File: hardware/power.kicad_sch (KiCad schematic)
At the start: 64 parts, among them IC1 LMR38020FDDAR, Q1 LMR51635XDDCR, Q2 LMR51635XDDCR, U3 LM1117-3.3

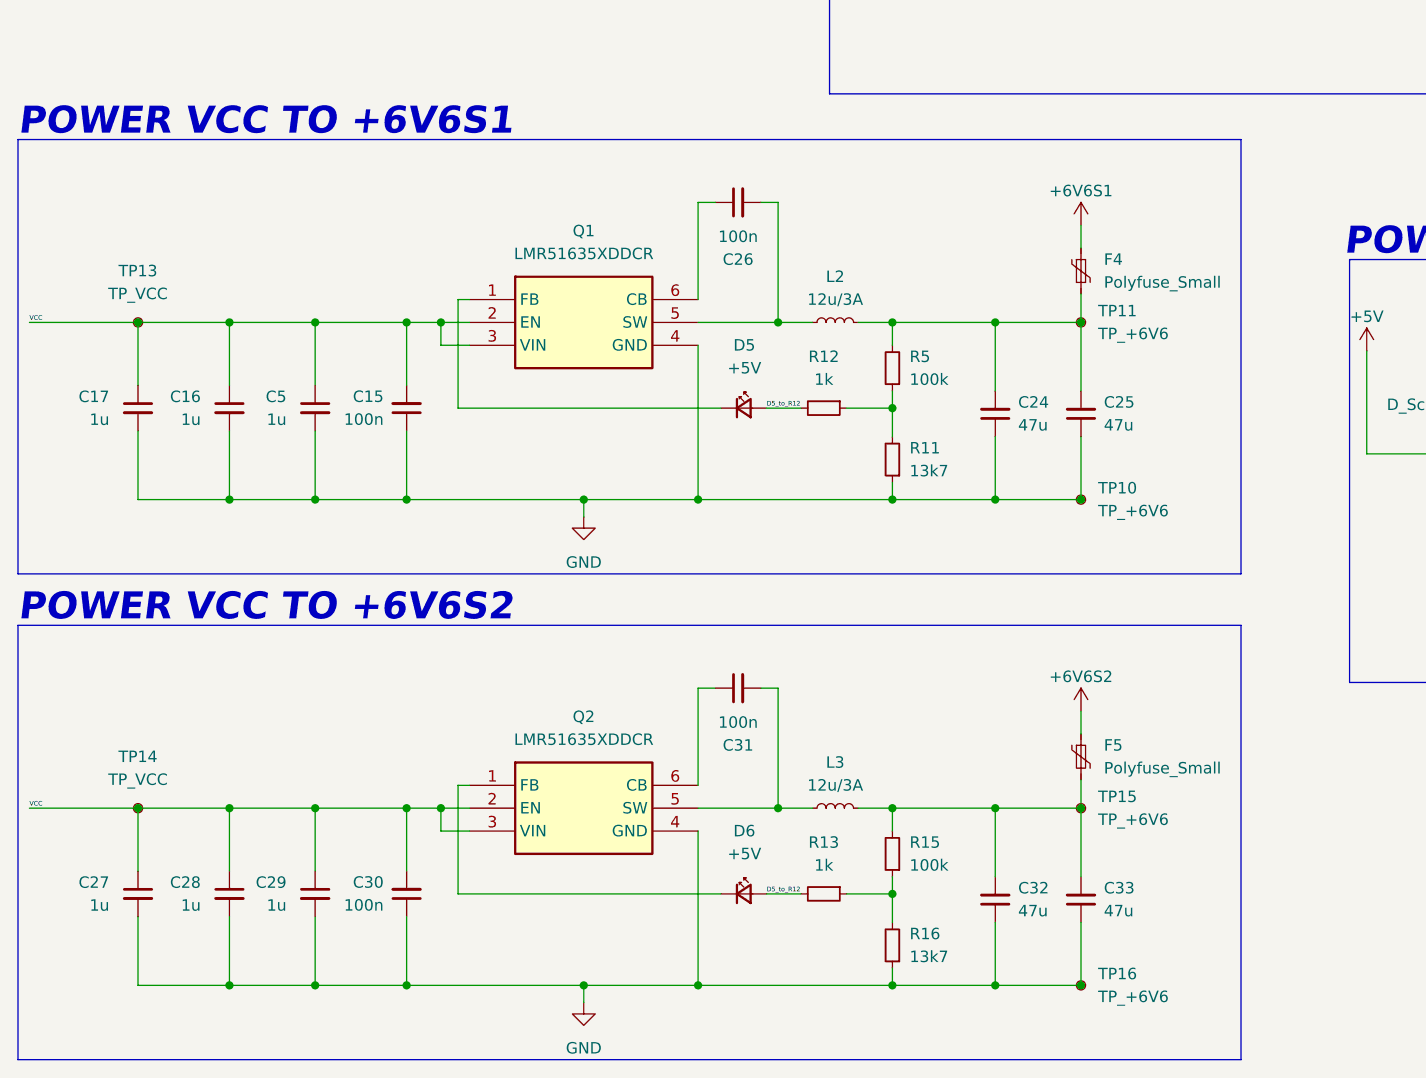
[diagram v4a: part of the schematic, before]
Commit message: power labels corrected
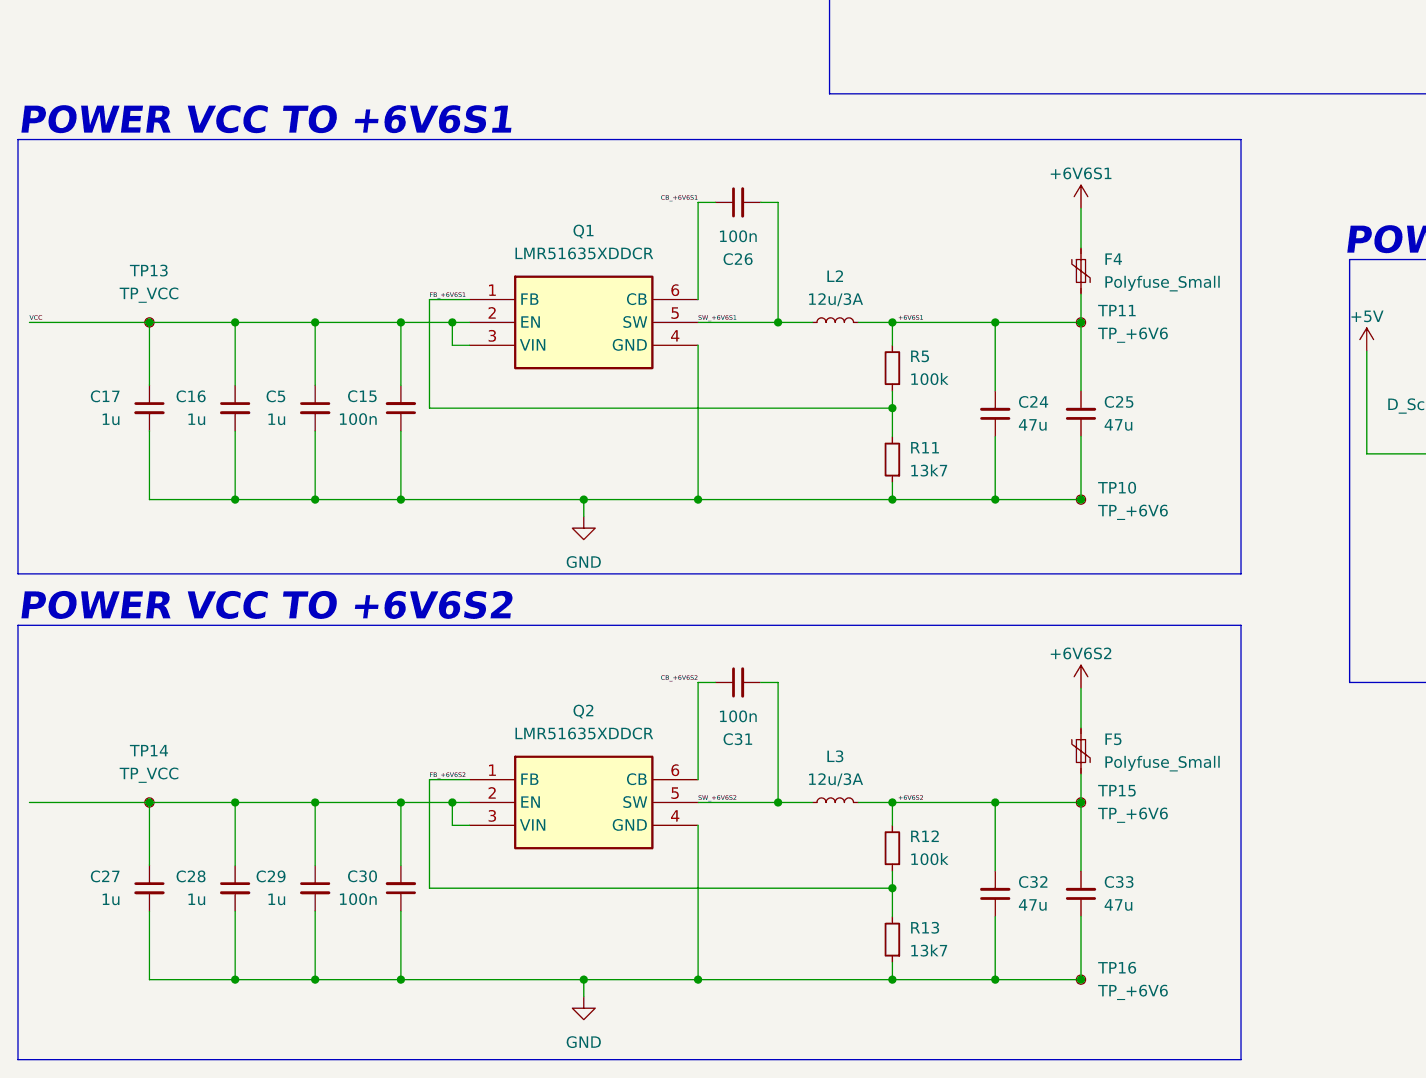
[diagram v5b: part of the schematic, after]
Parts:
- removed D5, D6: +5V, symbol Device:LED_Small
- removed R15: 100k, symbol Device:R_Small
- removed R16: 13k7, symbol Device:R_Small
- R12: value 1k -> 100k
- R13: value 1k -> 13k7
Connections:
- net +6V6S1: now also C24.2, C25.2, F4.2, L2.2, R5.2, TP11.1
- net +6V6S2: now also C32.2, C33.2, F5.2, L3.2, R12.2, TP15.1
- net GND: now also R13.1
- net VCC: no longer C27.1, C28.1, C29.1, C30.2, Q2.2 (EN), Q2.3 (VIN), TP14.1
- net FB_+6V6S1: now reaches Q1.1 (FB)
- net FB_+6V6S1: now also R11.2, R5.1
- net SW_+6V6S2: now reaches C31.2, L3.1, Q2.5 (SW)
- net CB_+6V6S1: now reaches C26.1, Q1.6 (CB)
- net SW_+6V6S1: now reaches C26.2, L2.1, Q1.5 (SW)
- net FB_+6V6S2: now reaches Q2.1 (FB)
- net FB_+6V6S2: now also R12.1, R13.2
- net CB_+6V6S2: now reaches C31.1, Q2.6 (CB)
- removed net D5_to_R12: R12.2, R13.2
- new net: C27.1, C28.1, C29.1, C30.2, Q2.2 (EN), Q2.3 (VIN), TP14.1
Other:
- moved on the sheet: C15, C16, C17, TP13

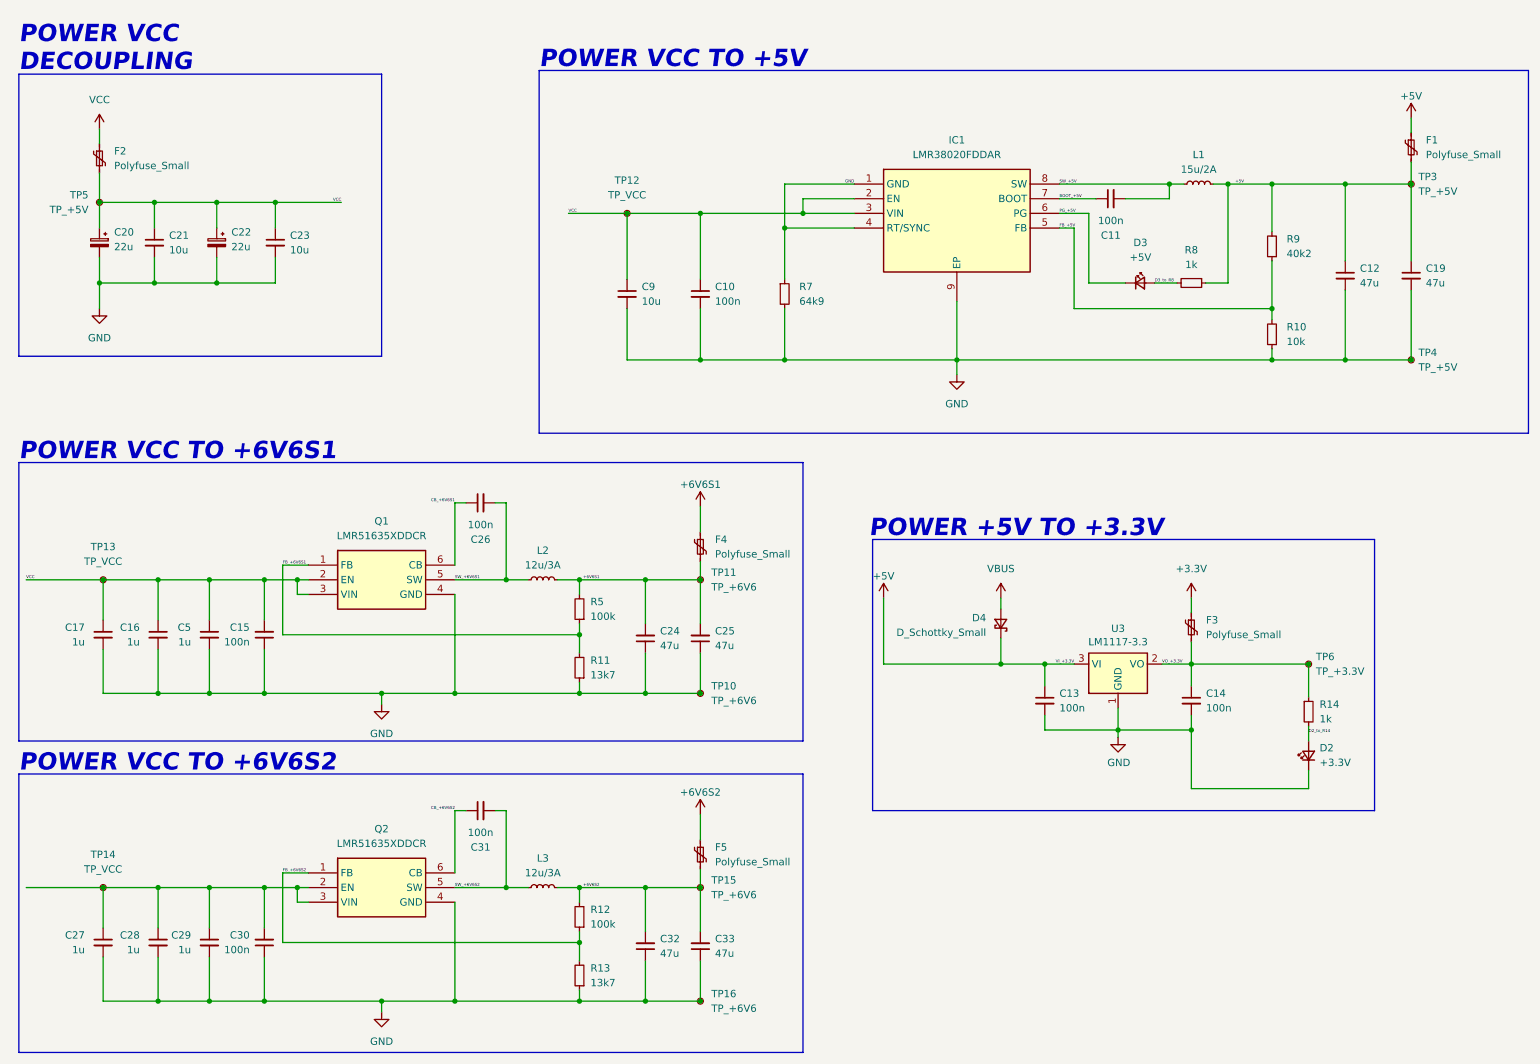
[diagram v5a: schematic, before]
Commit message: connectors - added, buses - todo
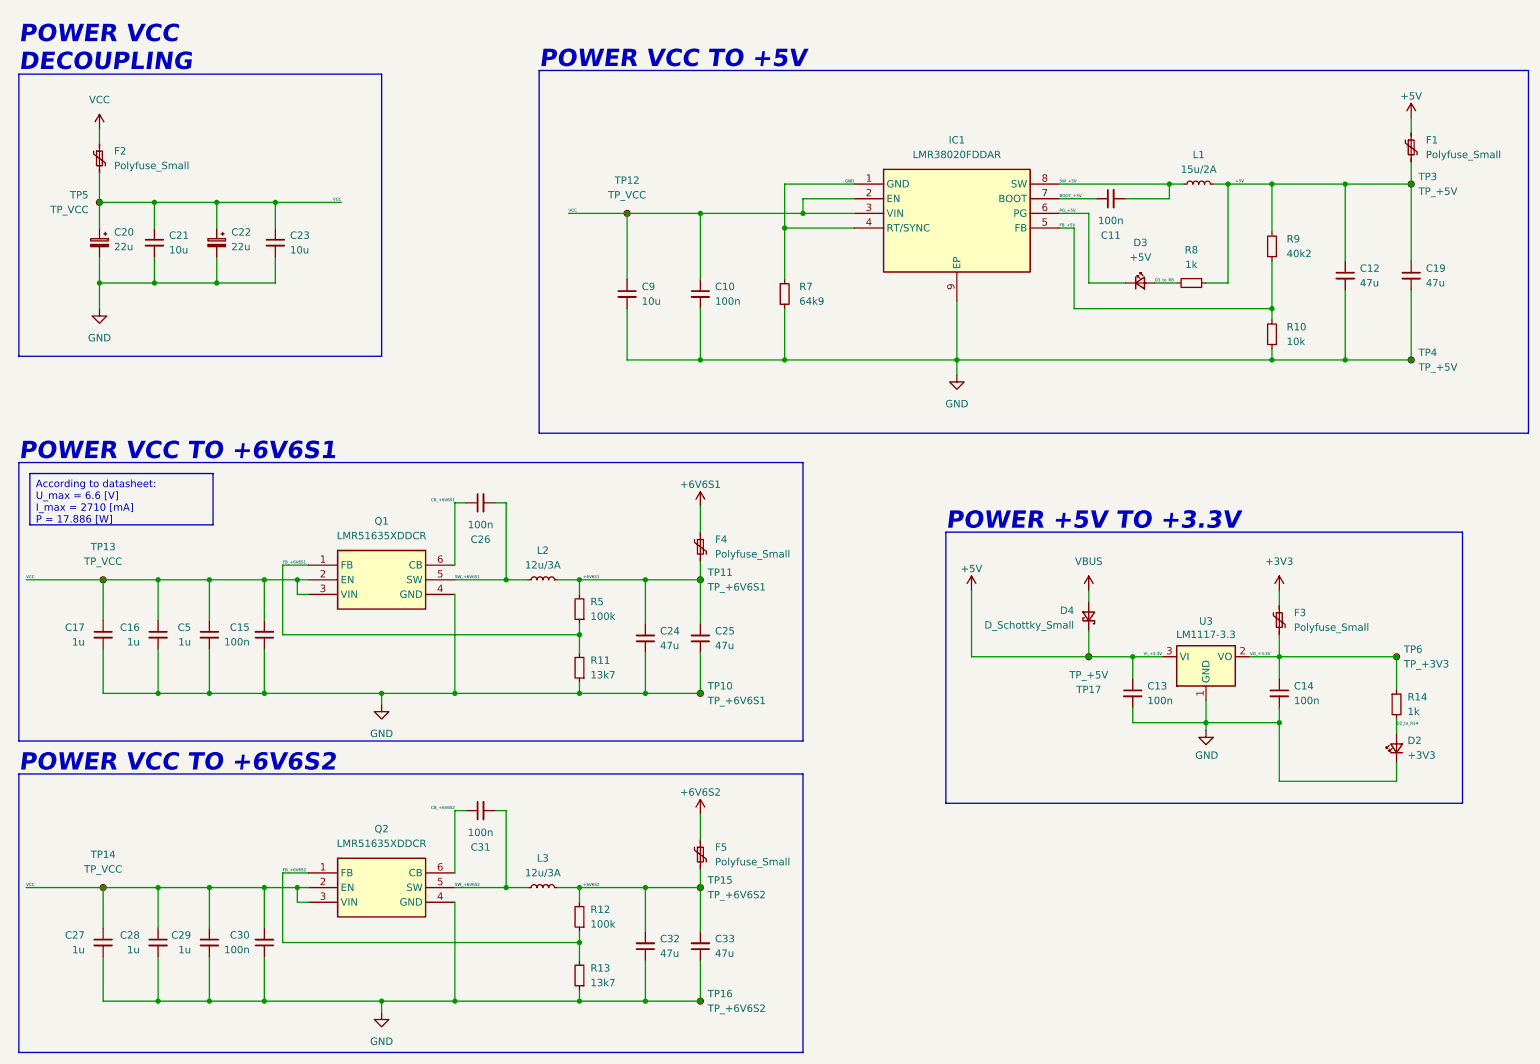
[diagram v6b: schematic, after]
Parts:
- added TP17: TP_+5V, symbol Connector:TestPoint_Small
- D2: value +3.3V -> +3V3
- TP10, TP11: value TP_+6V6 -> TP_+6V6S1
- TP15, TP16: value TP_+6V6 -> TP_+6V6S2
- TP5: value TP_+5V -> TP_VCC
- TP6: value TP_+3.3V -> TP_+3V3
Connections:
- net +5V: now also TP17.1
- net VCC: now also C27.1, C28.1, C29.1, C30.2, Q2.2 (EN), Q2.3 (VIN), TP14.1
- net +3.3V renamed +3V3
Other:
- moved on the sheet: C13, C14, D2, D4, F3, R14, TP6, U3

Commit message: Poprawione busy, brak errorow
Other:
- moved on the sheet: C10, C11, C15, C17, C20, C21, C22, C23, C24, C25, C27, C30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

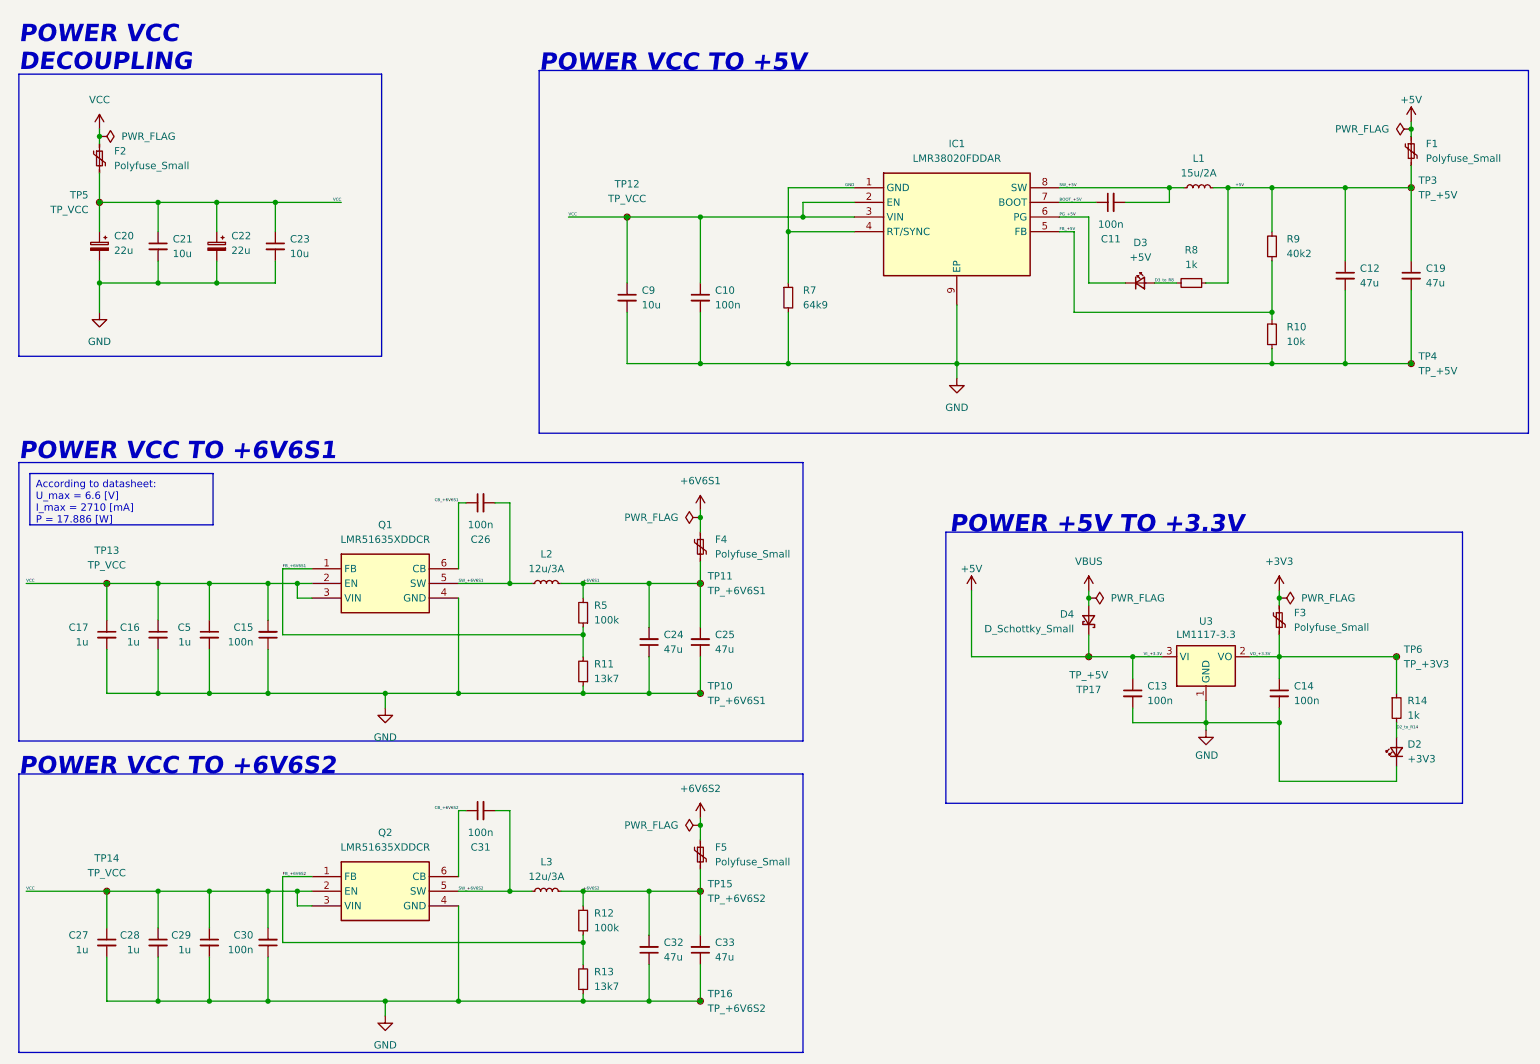
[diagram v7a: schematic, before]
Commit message: Footprints addes beside PWM connectors
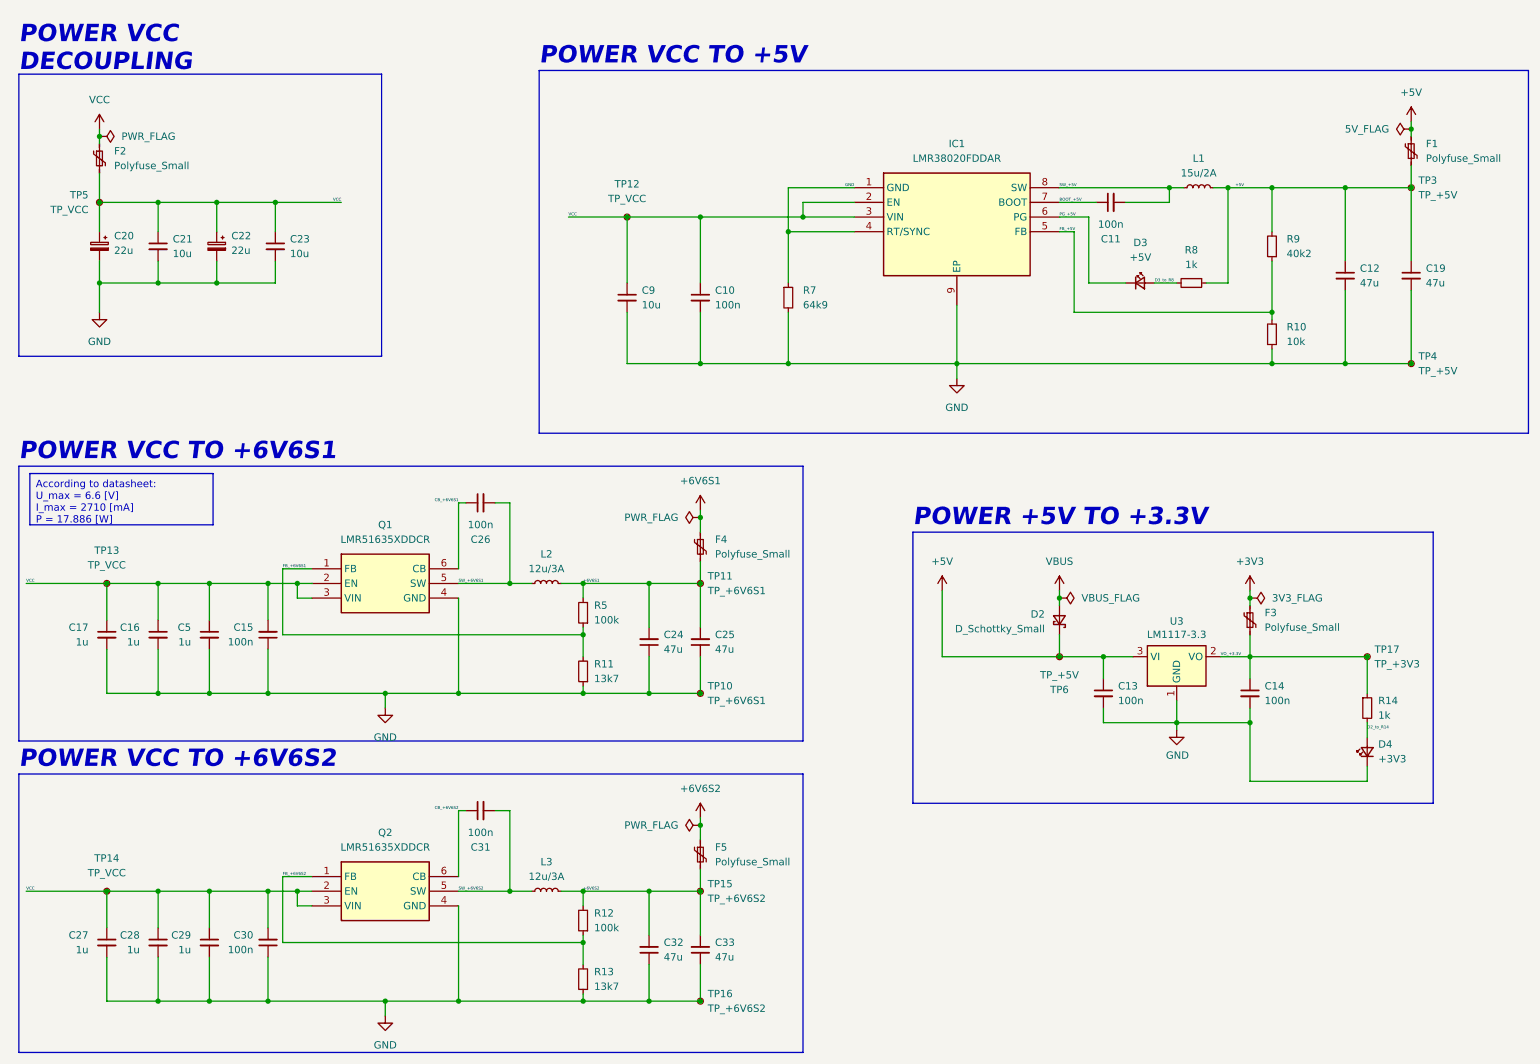
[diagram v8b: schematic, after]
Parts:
- removed D2: +3V3, symbol Device:LED_Small
- removed D4: D_Schottky_Small, symbol Device:D_Schottky_Small
- added D2: D_Schottky_Small, Diode_SMD:D_SOD-123, symbol Device:D_Schottky_Small
- added D4: +3V3, LED_SMD:LED_0603_1608Metric, symbol Device:LED_Small
- C10, C11, C12, C13, C14, C15, C16, C17, C19, C21, C23, C24, C25, C26, C27, C28, C29, C30, C31, C32, C33, C5, C9: footprint (none) -> Capacitor_SMD:C_0603_1608Metric_Pad1.08x0.95mm_HandSolder
- D3: footprint (none) -> LED_SMD:LED_0603_1608Metric
- F1, F2, F3, F4, F5: footprint (none) -> Fuse:Fuse_1206_3216Metric
- IC1: footprint SOIC127P600X170-9N -> SamacSys_Parts:SOIC127P600X170-9N
- L1: footprint (none) -> Inductor_SMD:L_Bourns-SRU1028_10.0x10.0mm
- L2, L3: footprint (none) -> SamacSys_Parts:SRR1206120ML
- Q1, Q2: footprint SOT95P280X110-6N -> SamacSys_Parts:SOT95P280X110-6N
- R10, R11, R12, R13, R14, R5, R7, R8, R9: footprint (none) -> Resistor_SMD:R_0603_1608Metric_Pad0.98x0.95mm_HandSolder
- TP10, TP11, TP12, TP13, TP14, TP15, TP16, TP3, TP4, TP5: footprint (none) -> TestPoint:TestPoint_Pad_1.0x1.0mm
- TP17: value TP_+5V -> TP_+3V3; footprint (none) -> TestPoint:TestPoint_Pad_1.0x1.0mm
- TP6: value TP_+3V3 -> TP_+5V; footprint (none) -> TestPoint:TestPoint_Pad_1.0x1.0mm
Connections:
- net +5V: now also TP6.1, D2.1 (K); no longer TP17.1
- net D2_to_R14: now also D4.2 (A)
- net GND: now also D4.1 (K)
- net VBUS: now also D2.2 (A)
- net VO_+3.3V: now also TP17.1; no longer TP6.1
